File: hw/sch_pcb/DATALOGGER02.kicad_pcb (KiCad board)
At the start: 4 copper layers, 101.1 x 60.5 mm, 163 parts, among them IC1 CY15B108QN-40SXI, IC2 FM3164-G, IC3 LTC4041EUFD#PBF, J1 HEADER_2x01_PARALLEL, J10 HEADER_2x05_PARALLEL, J11 HEADER_2x07_PARALLEL, J12 HEADER_2x05_PARALLEL, J13 HEADER_2x02_PARALLEL, J19 Conn_01x03_Male, J2 HEADER_2x01, J20 Conn_01x03_Male, J23 MCX, J24 HEADER_2x03_PARALLEL, J3 HEADER_2x03, J4 HEADER_2x03_PARALLEL, J5 HEADER_2x03_PARALLEL, J6 MCC-SD (kouka z modulu), J7 Conn_01x06_Female, J8 Conn_01x07_Female, J9 Conn_01x04_Female, Q1 DMP2045UQ-7, Q2 SIR424DP, Q3 SIR424DP, U1 ISL21080CIH320Z-TK, U10 TPS631000DRLR, U11 SX1262, U12 PE4259, U2 LM4041CIM3-1.2(neosazovat), U3 ATMEGA1284P-AU, U4 TXS0108EPW, U5 ICM-20948, U6 TPS22965-Q1, U7 MS5611-01BA, U8 MIC5504-1.8YM5-TR, U9 TPS631000DRLR, Y2 6pF crystal - 32.768kHz, Y3 32MHz, Y6 8MHz LFXTAL083138

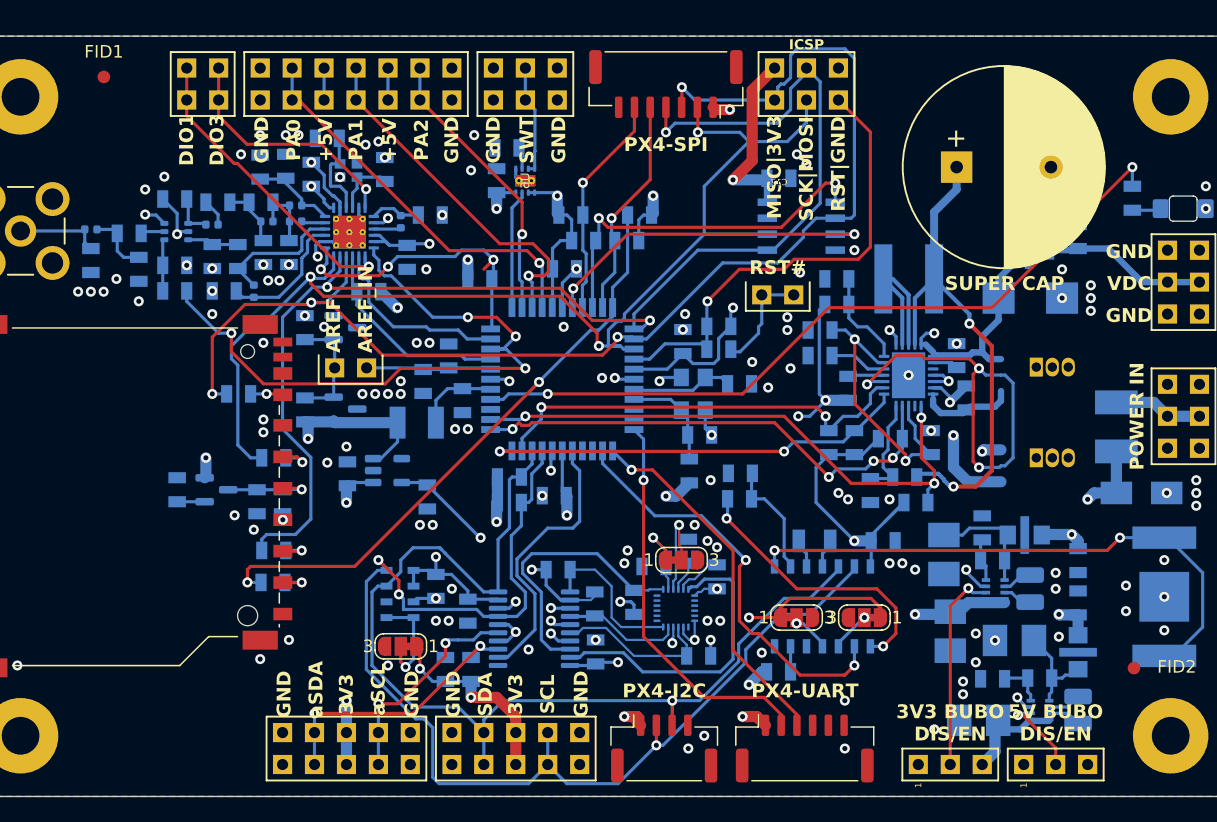
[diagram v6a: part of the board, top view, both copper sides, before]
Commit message: Update footprints. Improve layout Fix some DRC errors. Set components values matching inventory.
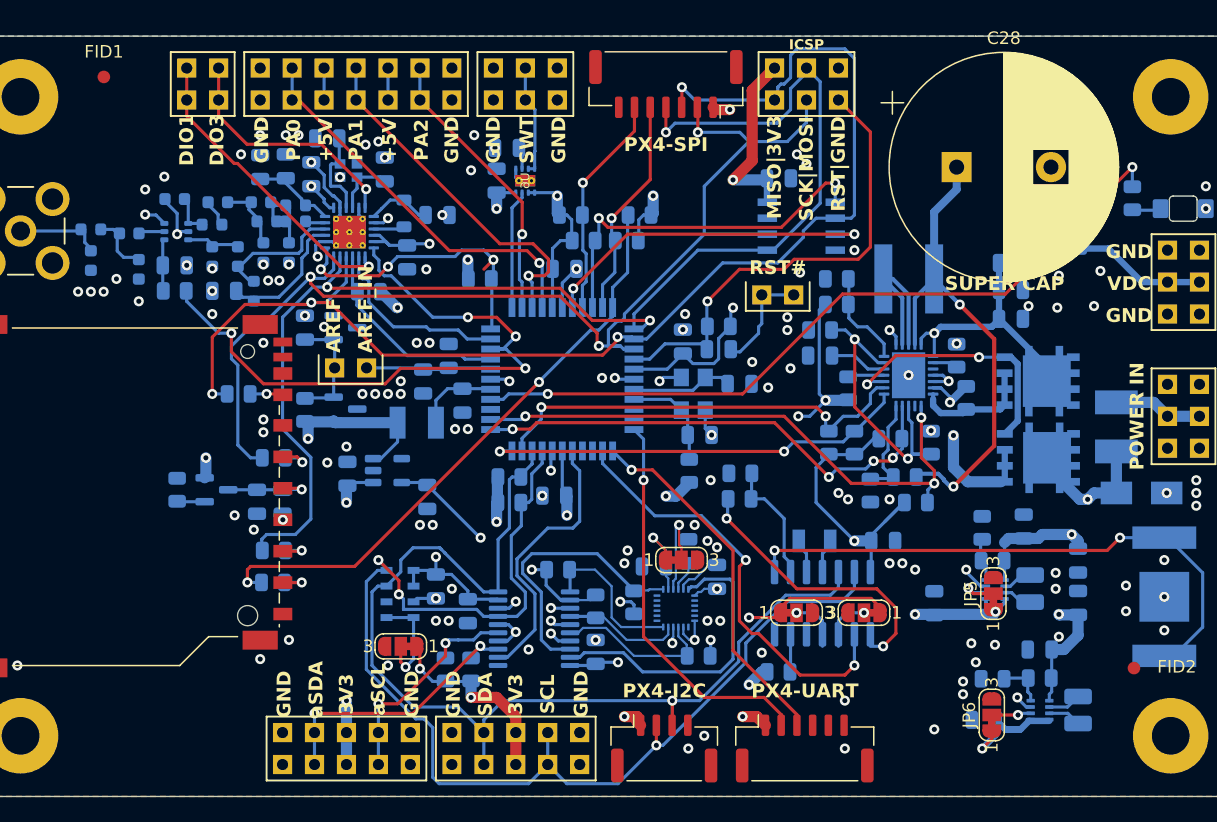
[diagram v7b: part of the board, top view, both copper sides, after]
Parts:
- removed C30, C35, C36: EMI_Filter_C, Mlab_L:FIR_0805
- removed C40: 22uF, Mlab_C:TantalC_SizeB_Reflow
- removed J19, J20: Conn_01x03_Male, Mlab_Pin_Headers:Straight_1x03
- added C11: 22uF, Capacitor_SMD:C_0805_2012Metric, B.Cu at (132.5, 130.8)
- added C12: 47uF, Capacitor_SMD:C_0805_2012Metric, B.Cu at (136.9, 125.2)
- added C13: 47uF, Capacitor_SMD:C_0805_2012Metric, B.Cu at (135.6, 115.4)
- added JP5: ModeSelect, Jumper:SolderJumper-3_P1.3mm_Bridged12_RoundedPad1.0x1.5mm_NumberLabels, F.Cu at (133.2, 120.8)
- added JP6: ModeSelect, Jumper:SolderJumper-3_P1.3mm_Bridged12_RoundedPad1.0x1.5mm_NumberLabels, F.Cu at (133.1, 130.4)
- C1, C10, C14, C15, C16, C17, C18, C19, C2, C20, C21, C22, C23, C24, C25, C26, C27, C3, C31, C32, C37, C38, C4, C41, C42, C43, C44, C45, C46, C47, C48, C5, C56, C6, C7, C8, C9: footprint Mlab_C:SMD-0805 -> Capacitor_SMD:C_0805_2012Metric
- C28: footprint Mlab_C:C_Radial_D16_L25_P7.5 -> Capacitor_THT:CP_Radial_D18.0mm_P7.50mm
- C29: value 100uF -> 47uF; footprint Mlab_C:TantalC_SizeC_Reflow -> Capacitor_SMD:C_0805_2012Metric
- C33: value 47uF -> 22uF; footprint Mlab_C:TantalC_SizeB_Reflow -> Capacitor_SMD:C_0805_2012Metric
- C34, C39: footprint Mlab_C:TantalC_SizeB_Reflow -> Capacitor_SMD:C_0805_2012Metric
- C49, C50, C51, C52, C53, C54, C55, C57, C58, C59: footprint Mlab_C:SMD-0805 -> Capacitor_SMD:C_0603_1608Metric
- IC2: footprint Mlab_IO:SOIC-14 -> Package_SO:SOIC-14_3.9x8.7mm_P1.27mm
- L10, L11, L6, L7, L8: footprint Inductor_SMD:L_0402_1005Metric -> Inductor_SMD:L_0603_1608Metric
- L5: footprint Inductor_SMD:L_0402_1005Metric -> Inductor_SMD:L_0805_2012Metric
- L9: value 2n5 -> 2n4; footprint Inductor_SMD:L_0402_1005Metric -> Inductor_SMD:L_0603_1608Metric
- Q2, Q3: value SIR424DP -> DMTH3002LPS; footprint Package_TO_SOT_THT:TO-92_Inline -> Mlab_T:D_POWERDI5060-8_6.0x5.1mm_P1.27mm
- R1, R10, R11, R14, R15, R16, R17, R18, R19, R2, R20, R21, R22, R23, R24, R25, R26, R27, R28, R29, R3, R30, R31, R32, R33, R34, R35, R36, R37, R38, R39, R40, R41, R42, R43, R44, R45, R46, R47, R48, R5, R6, R8, R9: footprint Mlab_R:SMD-0805 -> Resistor_SMD:R_0805_2012Metric
- moved C39 27.5 mm to (134.6, 96.6), turned to 0 degrees
- moved C34 23.8 mm to (134.6, 94.5), turned to 0 degrees
- moved C33 7.03 mm to (128.5, 121.5), turned to 90 degrees
- moved C29 2.26 mm to (134.6, 98.9)
- moved Q3 1.13 mm to (136.8, 103.9), turned to 180 degrees
- moved L5 0.71 mm to (86.4, 90.6)
- moved C43 0.57 mm to (89.0, 90.7)
- moved JP1 0.38 mm to (122.9, 122.3)
- moved JP2 0.38 mm to (117.6, 122.3)
- moved R15 0.21 mm to (101.6, 121.8)
- moved Q2 0.16 mm to (136.8, 110.0), turned to 180 degrees
- moved IC2 0.13 mm to (119.6, 121.5), turned to 90 degrees
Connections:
- C29 pad 1: Net-(IC3-VSYS_1) -> /Power_management/Vdc
- C33 pad 1: Net-(U9-VOUT) -> /Power_management/Vdc
- C34 pad 1: Net-(U10-VOUT) -> /Power_management/Vdc
- IC3 pad 1: Net-(IC3-VSYS_1) -> /Power_management/Vdc
- IC3 pad 24: Net-(IC3-VSYS_1) -> /Power_management/Vdc
- Q3 pad 3: Net-(IC3-VSYS_1) -> /Power_management/Vdc
- R38 pad 1: Net-(IC3-VSYS_1) -> /Power_management/Vdc
- R42 pad 1: Net-(U9-VOUT) -> +5V
- R44 pad 1: Net-(U10-VOUT) -> +3.3V
- U10 pad 1: Net-(U10-VOUT) -> +3.3V
- U9 pad 1: Net-(U9-VOUT) -> +5V
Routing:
- net /Power_management/Vdc: track 94.9 -> 131.4 mm, vias 1 -> 5
- net Net-(IC3-VSYS_1): track 25.8 -> 0.00 mm, vias 2 -> 0
- net Net-(JP5-C): track 16.1 -> 3.71 mm
- net /Power_management/igate: track 32.1 -> 20.9 mm, vias 3 -> 2
- net Net-(U10-VOUT): track 9.22 -> 0.00 mm
- net Net-(U9-VOUT): track 7.84 -> 0.00 mm
- net +5V: track 153.5 -> 161.0 mm
- net +3.3V: track 394.4 -> 400.5 mm
- net UNREG_POWER_INPUT: track 76.9 -> 80.6 mm, vias 6 -> 5
- net Net-(JP6-C): track 6.47 -> 3.15 mm
- net Net-(IC3-VIN): track 15.0 -> 17.5 mm
- net Net-(IC3-CLN): track 7.73 -> 9.98 mm
- net /Peripherals/A1: track 2.97 -> 4.36 mm
- net SCL_I2C: track 97.5 -> 98.7 mm
- net /Peripherals/A0: track 3.17 -> 4.33 mm
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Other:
- board text removed: "3V3 BUBO DIS/EN"
- board text removed: "5V BUBO DIS/EN"

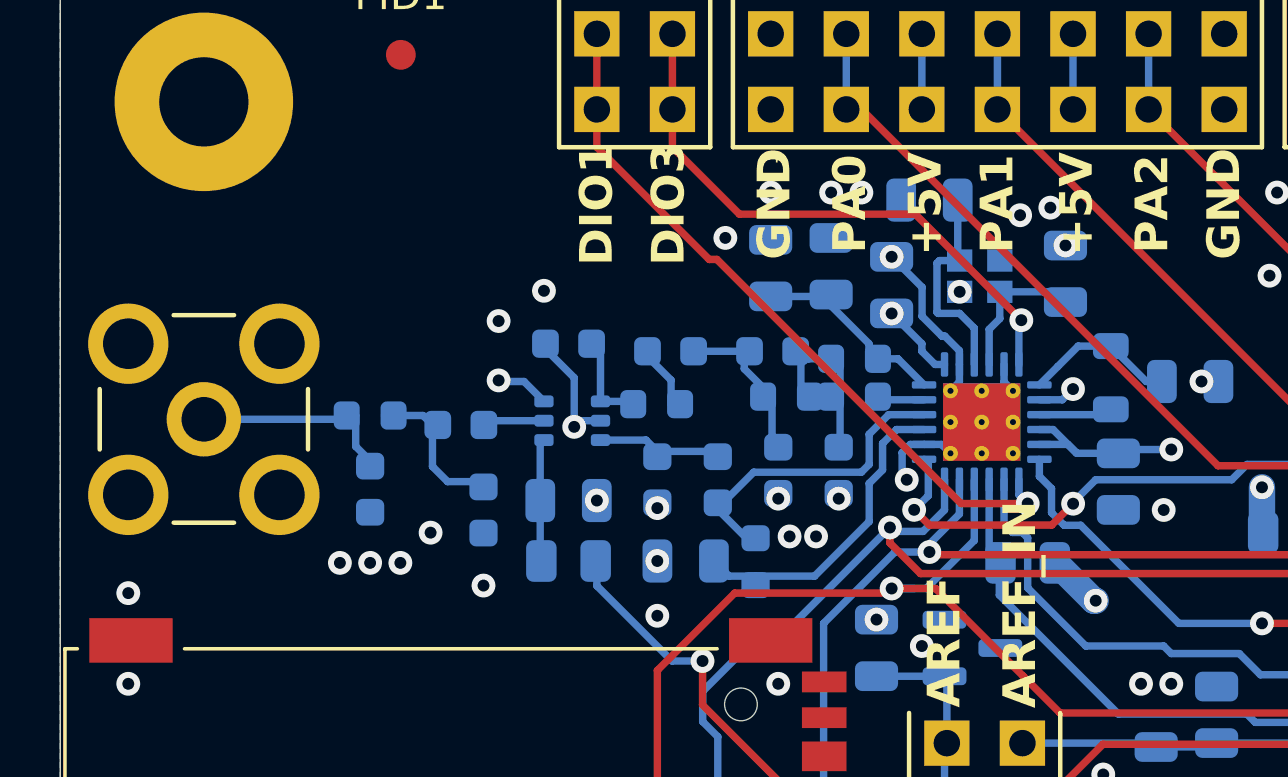
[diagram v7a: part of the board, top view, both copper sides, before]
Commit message: Fix component placement and layout of telemetry transceiver.
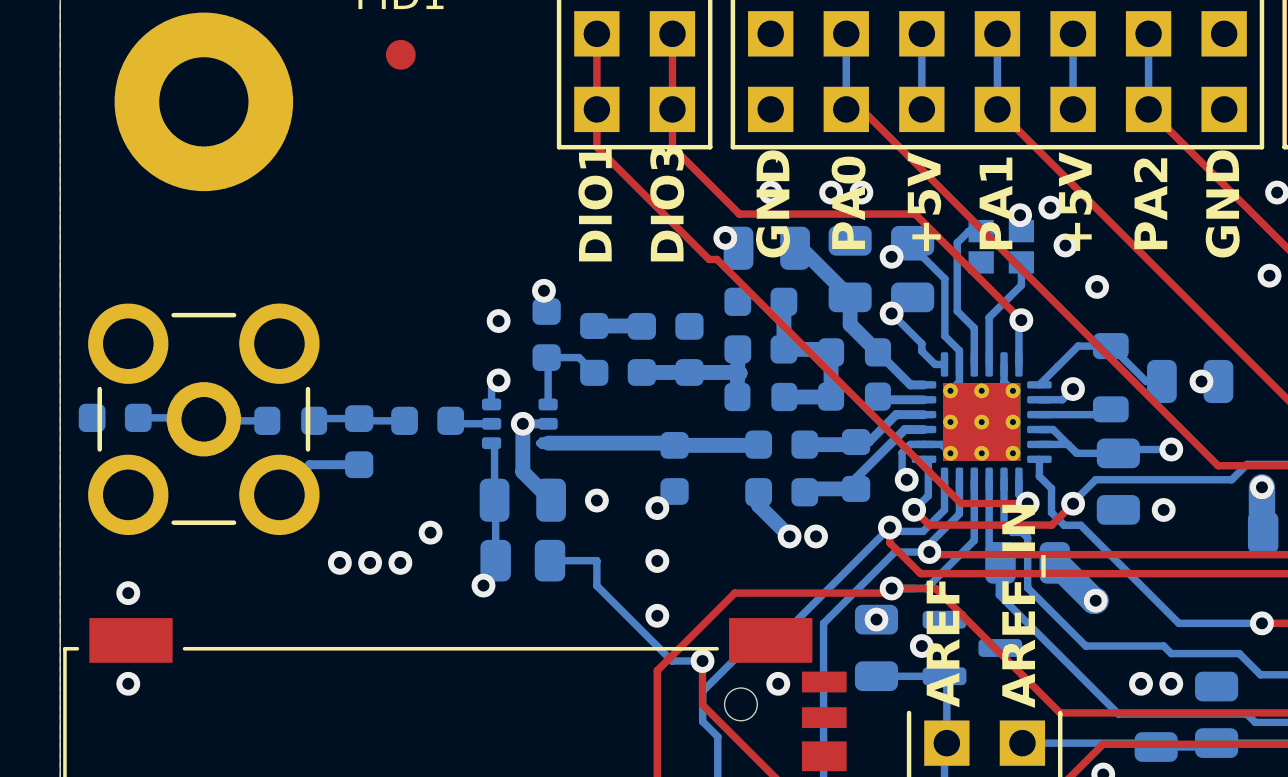
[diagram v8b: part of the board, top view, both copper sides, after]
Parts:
- removed C41, C42: -, Capacitor_SMD:C_0805_2012Metric
- C47: footprint Capacitor_SMD:C_0805_2012Metric -> Capacitor_SMD:C_0603_1608Metric
- moved C59 8.90 mm to (52.9, 91.9), turned to 0 degrees
- moved C50 6.24 mm to (74.6, 88.0), turned to 180 degrees
- moved C53 5.04 mm to (72.2, 89.6), turned to 90 degrees
- moved C58 4.77 mm to (61.1, 92.7)
- moved L6 4.68 mm to (77.8, 93.5)
- moved C47 3.97 mm to (75.3, 94.4)
- moved L10 2.79 mm to (69.0, 89.6), turned to -90 degrees
- moved L11 2.67 mm to (58.8, 92.0)
- moved C49 2.45 mm to (75.3, 92.8), turned to 0 degrees
- moved U12 1.76 mm to (66.5, 92.1)
- moved C56 1.54 mm to (66.6, 94.7)
- moved R47 1.54 mm to (66.6, 96.7)
- moved Y3 1.23 mm to (82.7, 86.2)
- moved C57 1.12 mm to (63.4, 92.0)
- moved C54 0.97 mm to (70.6, 89.6), turned to -90 degrees
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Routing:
- net Net-(U11-RFI_N): track 10.7 -> 4.43 mm
- net Net-(U11-RFI_P): track 10.6 -> 5.09 mm
- net GND: track 54.7 -> 59.9 mm, vias 140 -> 138
- net Net-(U12-RF2): track 4.10 -> 7.15 mm
- net Net-(C59-Pad2): track 6.88 -> 4.38 mm
- net Net-(C57-Pad1): track 5.06 -> 3.10 mm
- net Net-(U11-XTA): track 7.20 -> 5.43 mm
- net DIO_LORA: track 52.7 -> 54.3 mm
- net Net-(U11-XTB): track 4.94 -> 3.88 mm
- net +3.3V: track 400.5 -> 399.6 mm
- net Net-(C54-Pad1): track 2.18 -> 1.61 mm
- net Net-(C50-Pad1): track 5.76 -> 6.29 mm
